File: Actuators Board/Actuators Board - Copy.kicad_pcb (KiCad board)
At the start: 2 copper layers, 50 x 50 mm, 113 parts, among them IC1 BD62120AEFJ-E2, J1 Conn_01x05_Male, J10 Conn_01x02_Male, J2 Solenoid(Sol), J3 USB_C_Receptacle_USB2.0, J4 Conn_01x03_Male, J5 Conn_01x06_Male, J9 Conn_01x02_Male, Q1 MMDT2222A, Q2 SI2366DS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

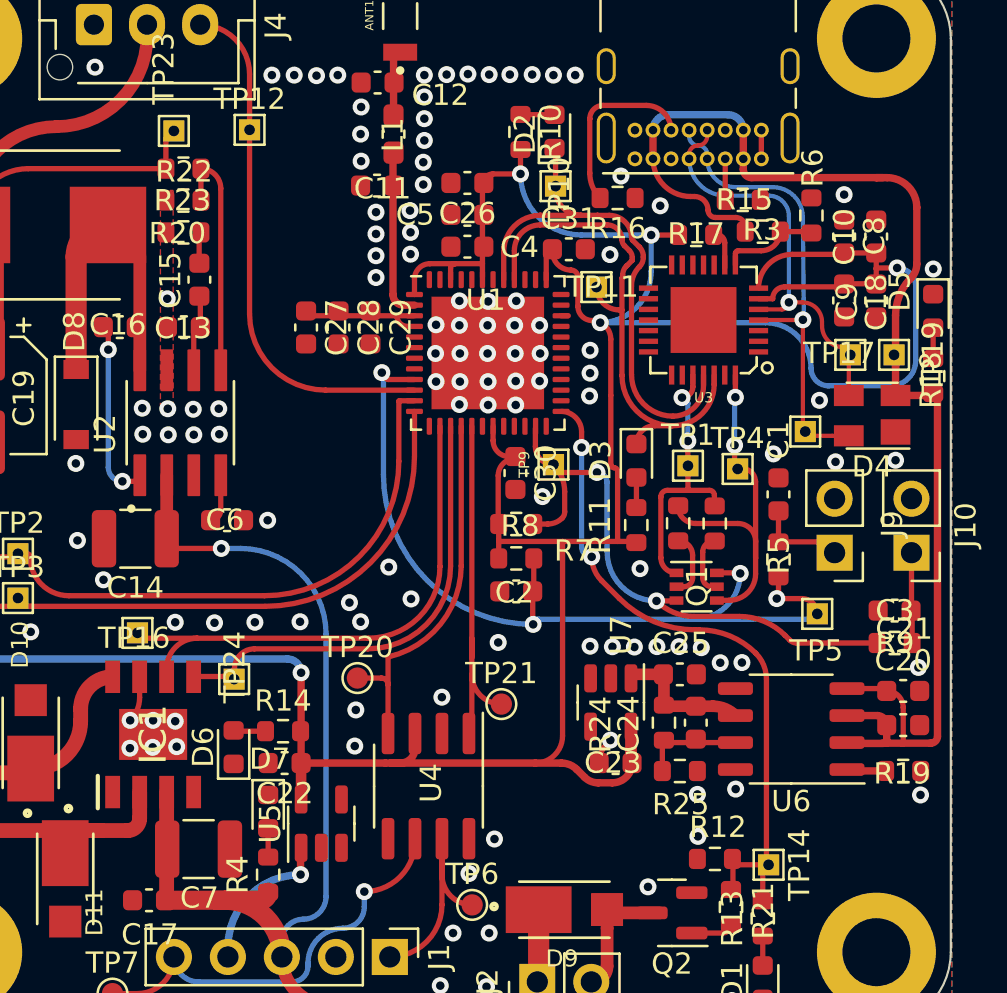
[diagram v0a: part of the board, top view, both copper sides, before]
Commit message: gnd vias for c25,c30,c18,c31 and ic1
trace for ic1
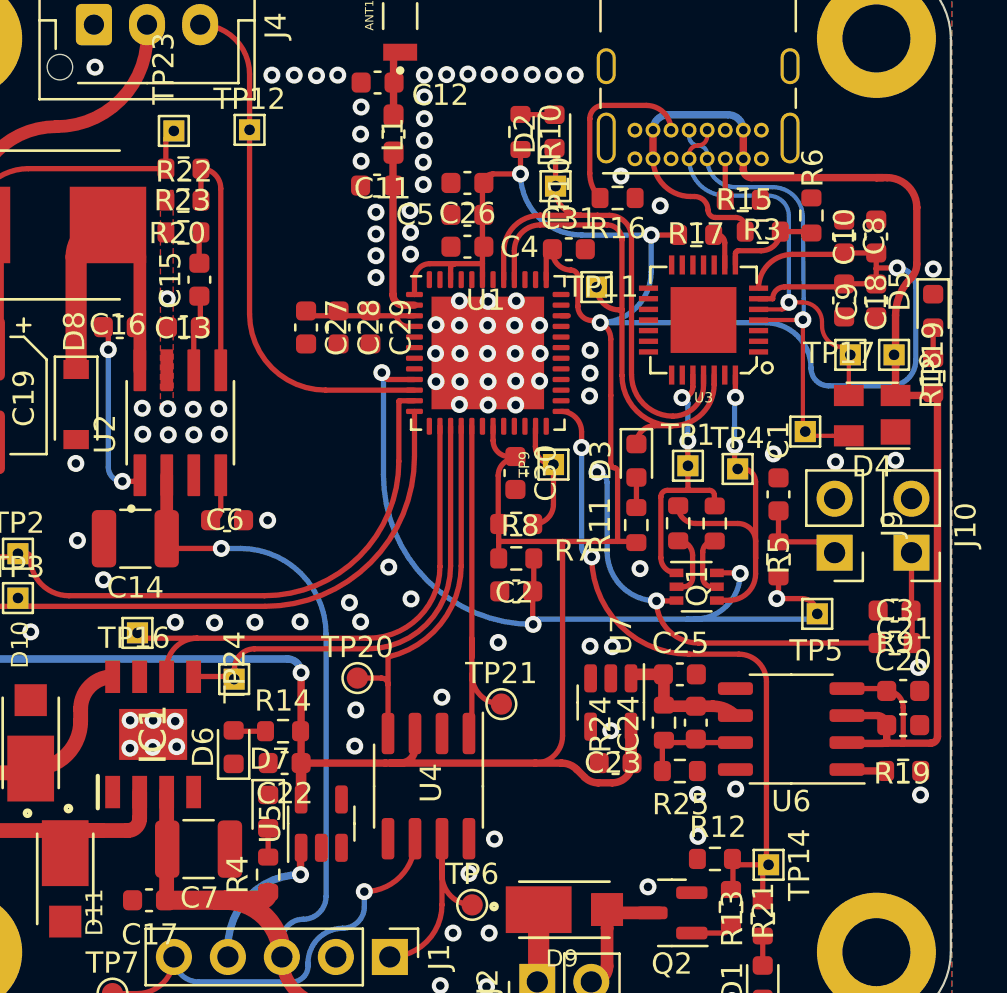
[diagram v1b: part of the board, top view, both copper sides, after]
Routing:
- net GND: track 5.11 -> 0.37 mm, vias 121 -> 111
- net /BOOT: track 28.4 -> 25.9 mm

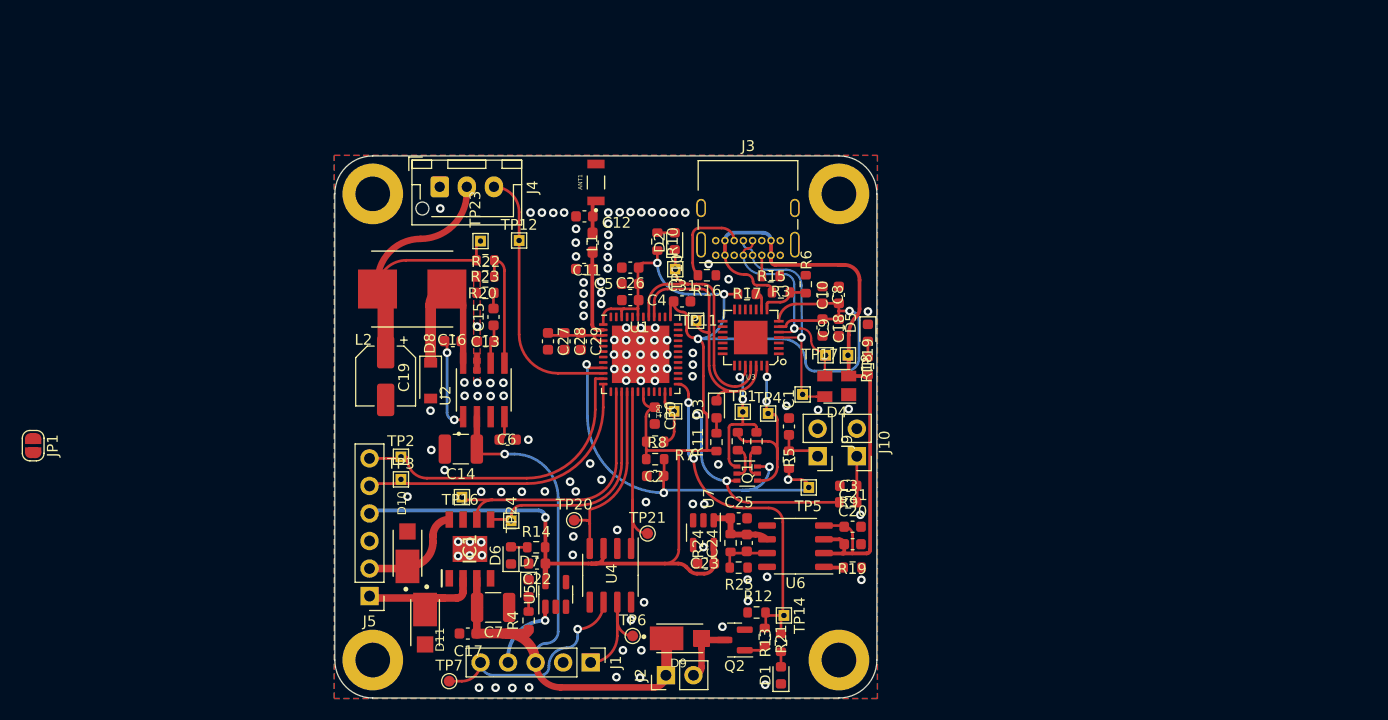
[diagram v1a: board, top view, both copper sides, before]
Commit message: SSR connector layout done in copy
copies made and moved pin for SSRGPIO in the schematic
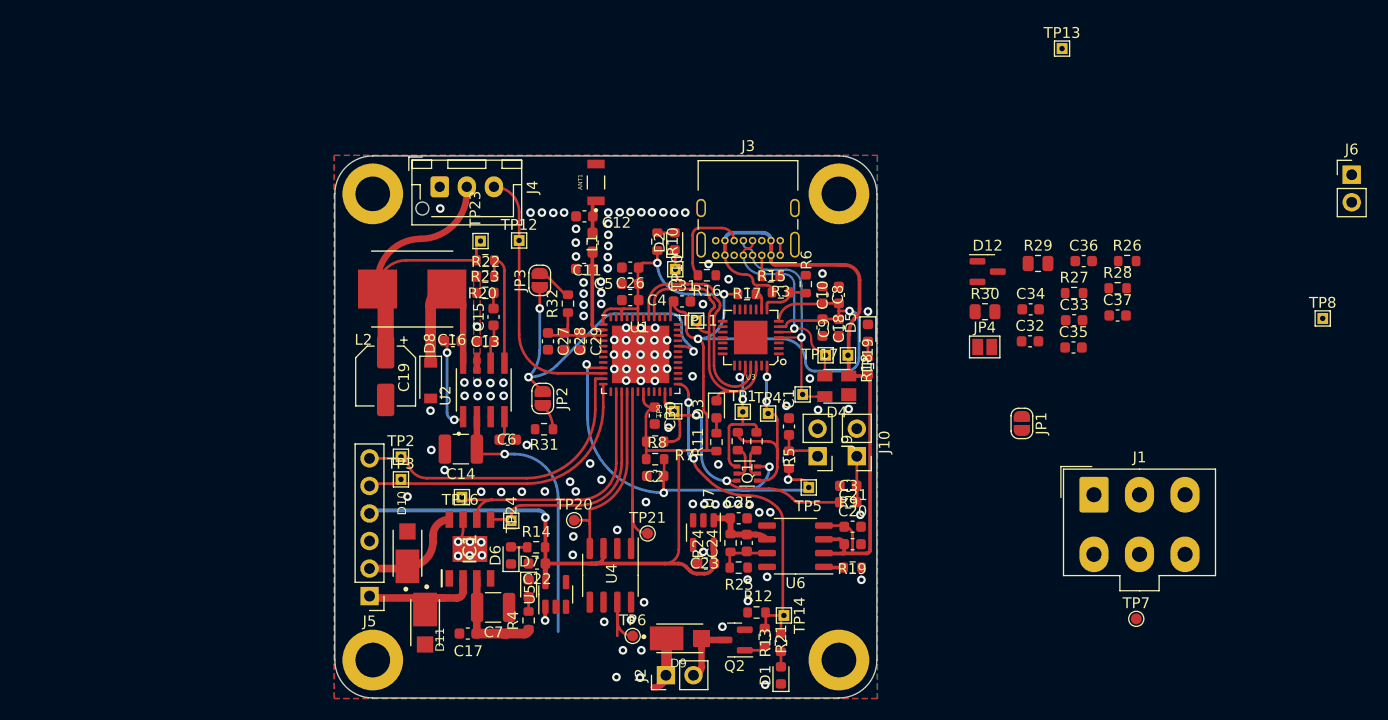
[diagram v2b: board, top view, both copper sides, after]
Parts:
- added C32: 160pF, Capacitor_SMD:C_0603_1608Metric, F.Cu at (119.1, 47.1)
- added C33: 100nF, Capacitor_SMD:C_0603_1608Metric, F.Cu at (123.2, 45.2)
- added C34: 10uF, Capacitor_SMD:C_0603_1608Metric, F.Cu at (119.2, 44.1)
- added C35: 0.1uF, Capacitor_SMD:C_0603_1608Metric, F.Cu at (123.1, 47.7)
- added C36: 220pF, Capacitor_SMD:C_0603_1608Metric, F.Cu at (124.1, 39.7)
- added C37: 220 pF, Capacitor_SMD:C_0603_1608Metric, F.Cu at (127.2, 44.7)
- added D12: SM712_SOT23, Package_TO_SOT_SMD:SOT-23, F.Cu at (115.2, 40.7)
- added J6: Conn_01x02_Female, Connector_PinHeader_2.54mm:PinHeader_1x02_P2.54mm_Vertical, F.Cu at (148.8, 31.7)
- added JP2: Pull-Down, Jumper:SolderJumper-2_P1.3mm_Open_RoundedPad1.0x1.5mm, F.Cu at (74.2, 52.4)
- added JP3: Pull-Up, Jumper:SolderJumper-2_P1.3mm_Open_RoundedPad1.0x1.5mm, F.Cu at (73.9, 41.5)
- added JP4: SolderJumper_2_Open, Jumper:SolderJumper-2_P1.3mm_Open_Pad1.0x1.5mm, F.Cu at (114.9, 47.6)
- added R26: 90, Resistor_SMD:R_0603_1608Metric, F.Cu at (128.1, 39.7)
- added R27: 90, Resistor_SMD:R_0603_1608Metric, F.Cu at (123.2, 42.6)
- added R28: 10k, Resistor_SMD:R_0603_1608Metric, F.Cu at (127.2, 42.2)
- added R29: 60, Resistor_SMD:R_0805_2012Metric, F.Cu at (119.9, 39.9)
- added R30: 60, Resistor_SMD:R_0805_2012Metric, F.Cu at (115.0, 44.4)
- added R31: 10k, Resistor_SMD:R_0603_1608Metric, F.Cu at (74.3, 55.2)
- added R32: 10k, Resistor_SMD:R_0603_1608Metric, F.Cu at (76.5, 43.6)
- added TP13: TestPoint, TestPoint:TestPoint_THTPad_1.0x1.0mm_Drill0.5mm, F.Cu at (122.1, 20.1)
- added TP8: TestPoint, TestPoint:TestPoint_THTPad_1.0x1.0mm_Drill0.5mm, F.Cu at (146.1, 45.0)
- J1: footprint Connector_PinHeader_2.54mm:PinHeader_1x05_P2.54mm_Vertical -> Connector_Molex:Molex_Mini-Fit_Jr_5566-06A_2x03_P4.20mm_Vertical
- moved JP1 91.2 mm to (118.4, 54.7)
- moved TP7 63.6 mm to (128.9, 72.7)
- moved J1 48.9 mm to (125.0, 61.2), turned to 0 degrees
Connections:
- J1 pad 1: /CAN_HIGH -> GND
- J1 pad 3: +24V -> Net-(J1-Pad3)
- J1 pad 4: Net-(J1-Pad4) -> +24V
- J1 pad 5: /CAN_LOW -> /CAN_HIGH
- U1 pad 32: unconnected-(U1-Pad32) -> /SSRGPIO
- U4 pad 1: /CAN_TX -> Net-(C32-Pad2)
- U4 pad 4: /CAN_RX -> Net-(R27-Pad2)
- U4 pad 5: unconnected-(U4-Pad5) -> /CAN-BUS/Vref
- U4 pad 8: GND -> Net-(R28-Pad1)
- U5 pad 1: Net-(J1-Pad4) -> Net-(J1-Pad3)
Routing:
- net /SSRGPIO: track 0.00 -> 31.7 mm, vias 0 -> 3
- net +24V: track 63.6 -> 42.7 mm
- net /CAN_LOW: track 19.8 -> 0.11 mm
- net Net-(J1-Pad4): track 6.97 -> 0.00 mm, vias 1 -> 0
- net GND: track 0.37 -> 5.11 mm, vias 111 -> 115
- net /CAN_HIGH: track 10.7 -> 6.98 mm
- net Net-(JP3-Pad2): track 0.00 -> 3.39 mm
- net /BOOT: track 25.9 -> 28.4 mm
- net Net-(JP2-Pad2): track 0.00 -> 2.44 mm
- net +3V3: track 154.6 -> 156.5 mm
- net Net-(J1-Pad3): track 0.00 -> 1.28 mm, vias 0 -> 1
